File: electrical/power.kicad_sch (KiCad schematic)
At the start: 33 parts

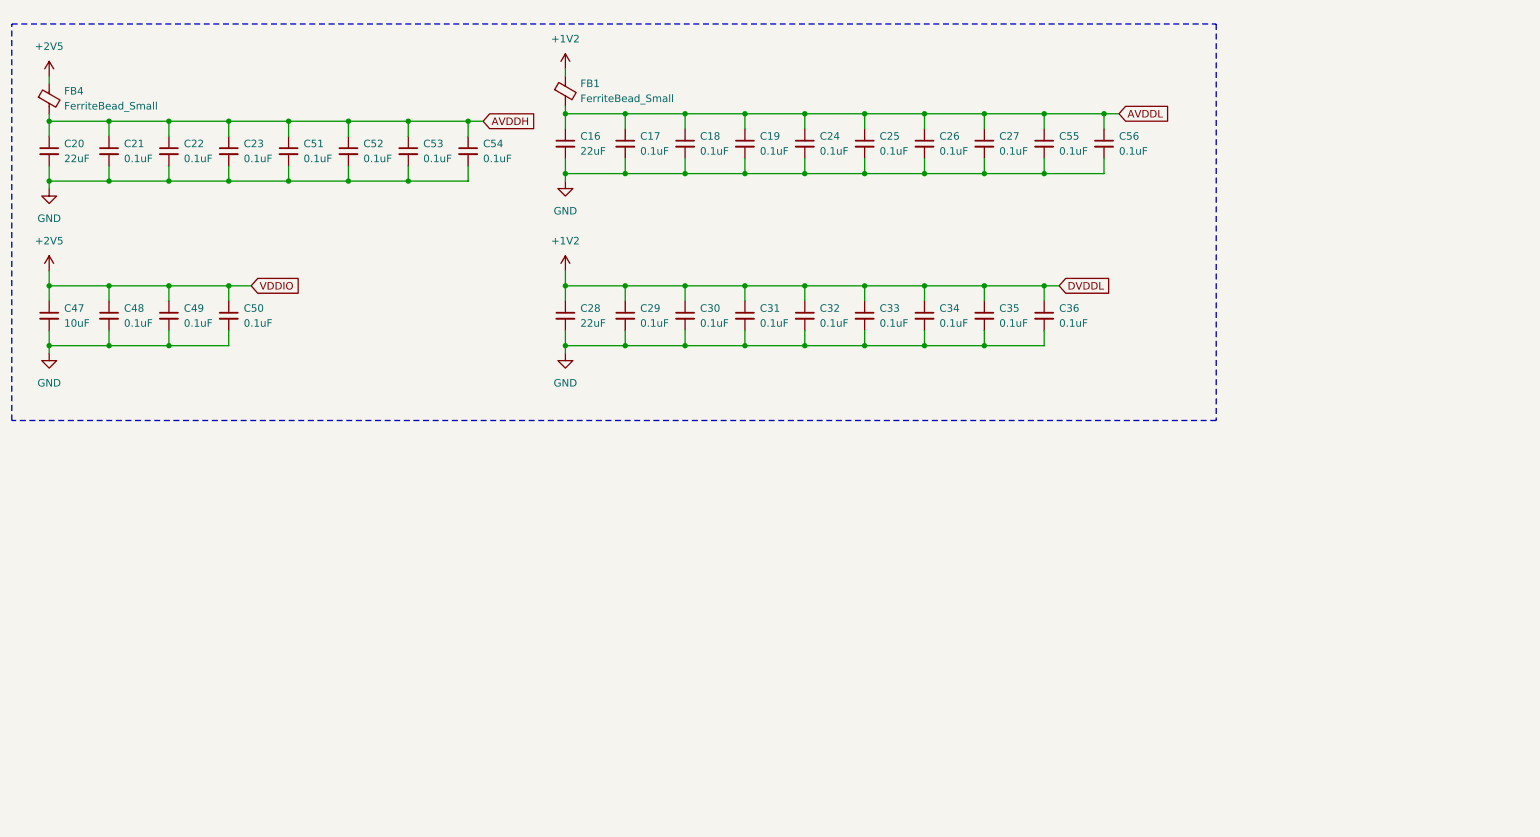
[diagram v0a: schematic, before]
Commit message: 2V5, 1V2 Buck converters
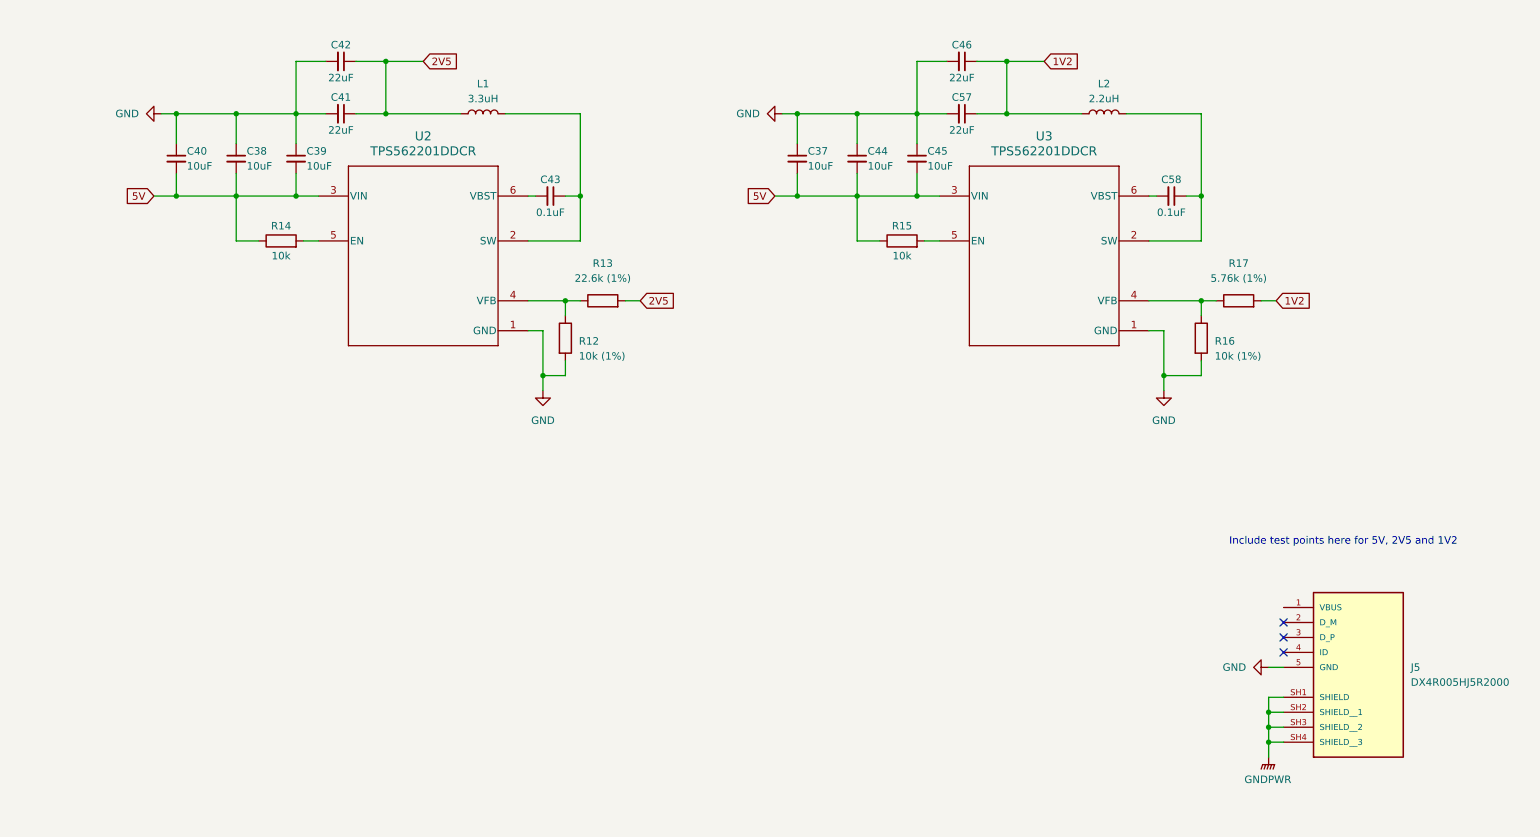
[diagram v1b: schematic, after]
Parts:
- removed C16, C20, C28: 22uF, symbol Device:C_Small
- removed C17, C18, C19, C21, C22, C23, C24, C25, C26, C27, C29, C30, C31, C32, C33, C34, C35, C36, C48, C49, C50, C51, C52, C53, C54, C55, C56: 0.1uF, symbol Device:C_Small
- removed C47: 10uF, symbol Device:C_Small
- removed FB1, FB4: FerriteBead_Small, symbol Device:FerriteBead_Small
- added C37, C38, C39, C40, C44, C45: 10uF, symbol Device:C_Small
- added C41, C42, C46, C57: 22uF, symbol Device:C_Small
- added C43, C58: 0.1uF, symbol Device:C_Small
- added J5: DX4R005HJ5R2000, DX4R005HJ5R2000:JAE_DX4R005HJ5R2000, symbol DX4R005HJ5R2000:DX4R005HJ5R2000
- added L1: 3.3uH, symbol Device:L
- added L2: 2.2uH, symbol Device:L
- added R12, R16: 10k (1%), symbol Device:R
- added R13: 22.6k (1%), symbol Device:R
- added R14, R15: 10k, symbol Device:R
- added R17: 5.76k (1%), symbol Device:R
- added U2, U3: TPS562201DDCR, DDC0006A_N, symbol TPS562201DDCR:TPS562201DDCR
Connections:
- net GND: now also C37.1, C38.1, C39.1, C40.1, C41.2, C42.2, C44.1, C45.1, C46.2, C57.2, J5.5 (GND), R12.2, R16.2, U2.1 (GND), U3.1 (GND)
- new net: C58.1, L2.2, U3.2 (SW)
- new net: C58.2, U3.6 (VBST)
- new net: C43.1, L1.2, U2.2 (SW)
- new net: C43.2, U2.6 (VBST)
- new net: R14.2, U2.5 (EN)
- new net: R12.1, R13.1, U2.4 (VFB)
- new net: R16.1, R17.1, U3.4 (VFB)
- new net: R15.2, U3.5 (EN)
- new net 1V2: C46.1, C57.1, L2.1, R17.2
- new net 2V5: C41.1, C42.1, L1.1, R13.2
- new net 5V: C37.2, C38.2, C39.2, C40.2, C44.2, C45.2, R14.1, R15.1, U2.3 (VIN), U3.3 (VIN)
- new net GNDPWR: J5.SH1 (SHIELD), J5.SH2 (SHIELD__1), J5.SH3 (SHIELD__2), J5.SH4 (SHIELD__3)
- no-connect marks 0 -> 3
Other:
- note added: "Include test points here for 5V, 2V5 and 1V2"

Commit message: Micro B + Header for eMMC flash
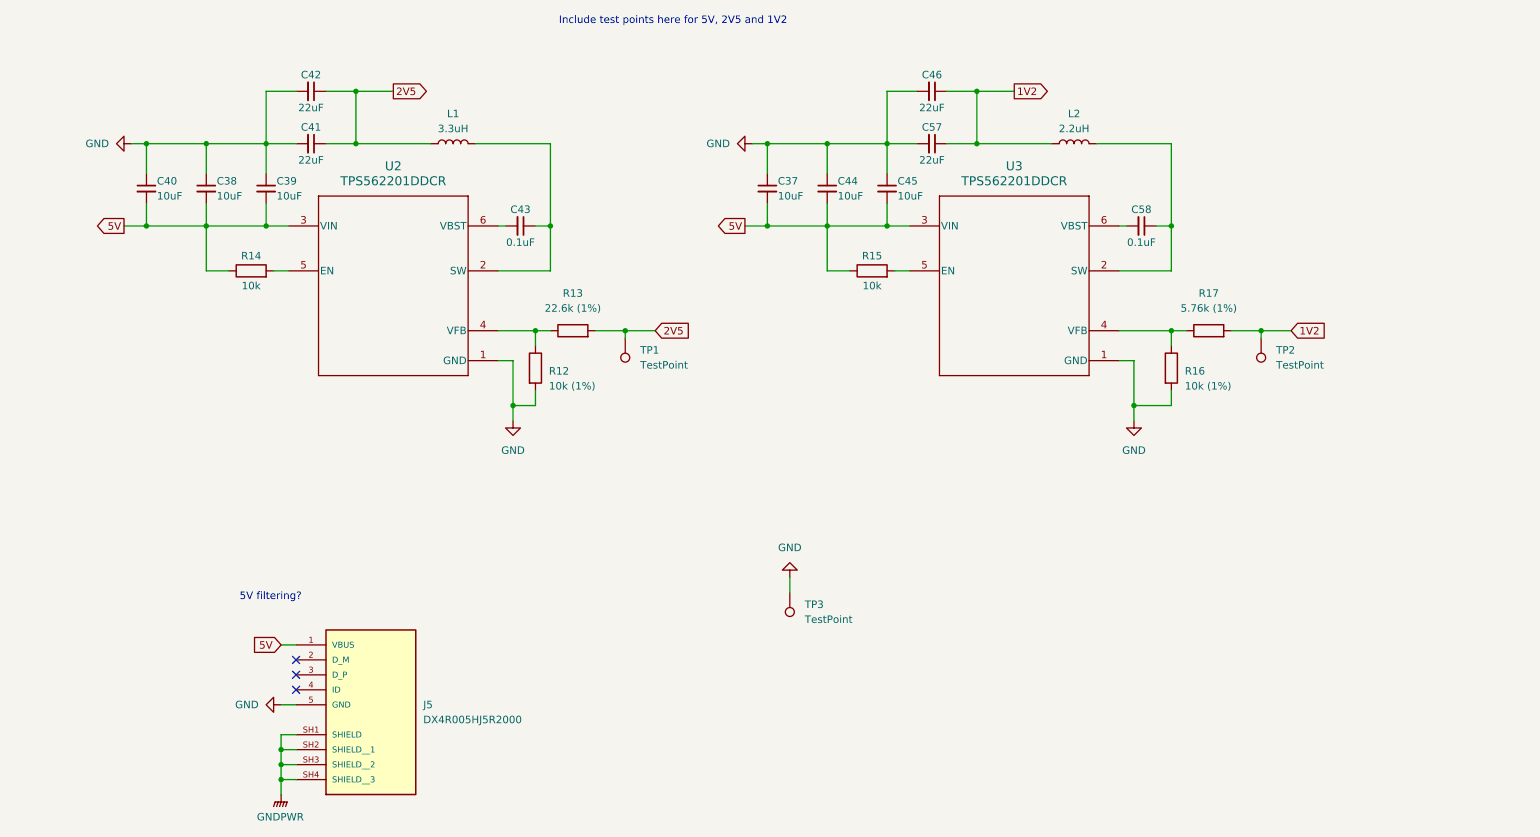
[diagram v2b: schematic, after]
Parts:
- added TP1, TP2, TP3: TestPoint, symbol Connector:TestPoint
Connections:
- net 1V2: now also TP2.1
- net 2V5: now also TP1.1
- net 5V: now also J5.1 (VBUS)
- net GND: now also TP3.1
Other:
- note added: "5V filtering?"
- title: (none) -> Network Tap
- moved on the sheet: C37, C38, C39, C40, C41, C42, C43, C44, C45, C46, C57, C58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
